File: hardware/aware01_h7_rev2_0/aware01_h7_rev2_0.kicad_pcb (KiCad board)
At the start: 4 copper layers, 46 x 110 mm, 155 parts, among them IC1 587-2054-127F, IC2 587-2054-127F, IC3 587-2054-127F, IC4 587-2054-127F, IC5 TLV320AIC3204IRHBR, J1 Conn_02x07_Odd_Even, J10 GATE4_IN, J11 CV2_IN, J12 CV3_IN, J13 V/OCT_IN, J14 CV1_IN, J2 Conn_02x05_Odd_Even, J3 InL, J4 InR, J5 OutL, J6 OutR, J7 GATE1_IN, J8 GATE2_IN, J9 GATE3_IN, Q1 MMBT3904, Q2 MMBT3904, Q3 MMBT3904, Q4 MMBT3904, SW1 SW_Push, SW2 SW_Push, U1 LMR50410Y5FQDBVRQ1, U10 NE5532DRG4, U11 NE5532DRG4, U12 OPA2322AIDR, U13 OPA2322AIDR, U2 LM1117MP-3.3, U4 STM32H7A3RITx, U5 LM4040DIM3X-10, U6 10k, U7 10k, U8 10k, U9 10k, Y1 WE-XTAL 24.0MHz 50ppm

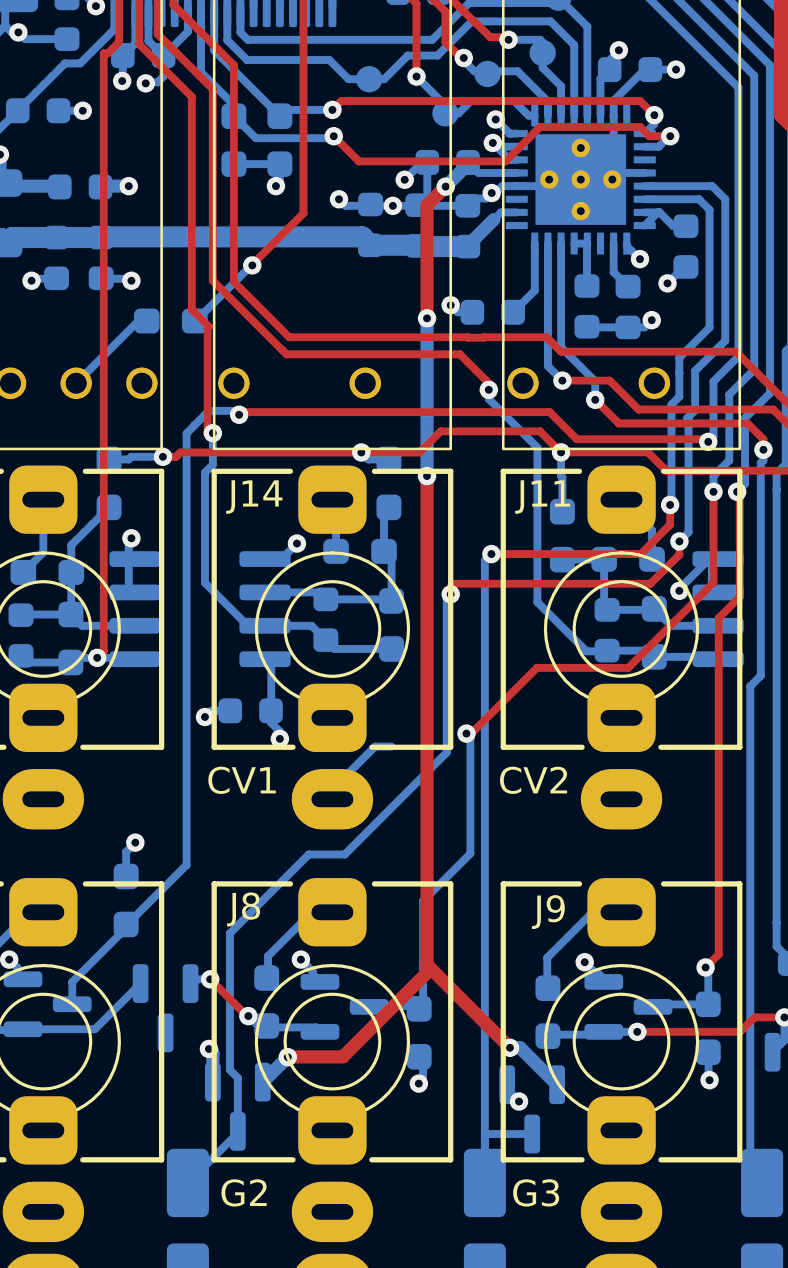
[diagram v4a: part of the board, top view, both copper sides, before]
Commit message: hardware: change clamping reference to codec AVDD
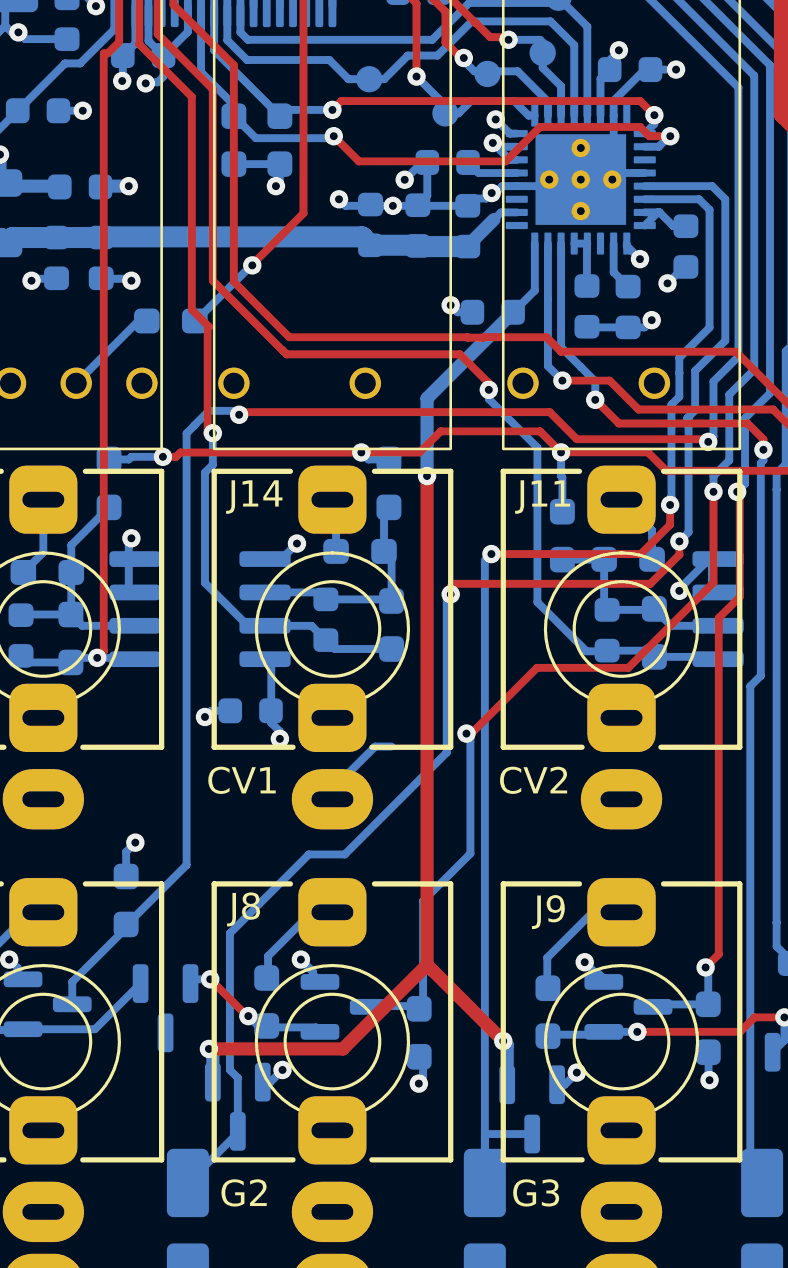
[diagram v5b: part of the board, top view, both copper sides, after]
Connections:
- C38 pad 2: DVDD -> Net-(IC5-DVDD)
- C41 pad 2: Net-(IC5-AVDD) -> AVDD
- D4 pad 1: GND -> AVDD
- D4 pad 2: DVDD -> GND
- D5 pad 1: GND -> AVDD
- D5 pad 2: DVDD -> GND
- IC5 pad 24: Net-(IC5-AVDD) -> AVDD
- IC5 pad 29: DVDD -> Net-(IC5-DVDD)
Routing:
- net DVDD: track 48.3 -> 0.00 mm, vias 5 -> 0
- net AVDD: track 0.00 -> 45.8 mm, vias 0 -> 3
- net Net-(IC5-AVDD): track 2.96 -> 0.00 mm
- net Net-(IC5-DVDD): track 0.00 -> 2.09 mm
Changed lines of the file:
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@@
 	(net 13 "Net-(C23-Pad2)")
 	(net 14 "/I2S1_CK")
-	(net 15 "DVDD")
+	(net 15 "Net-(IC5-DVDD)")
 	(net 16 "Net-(IC5-IN2_L)")
 	(net 17 "/UART_Rx")
-	(net 18 "Net-(IC5-AVDD)")
+	(net 18 "AVDD")
 	(net 19 "Net-(IC5-REF)")
 	(net 20 "/FADER1_IN")
@@
 			(layers "B.Cu" "B.Mask" "B.Paste")
 			(roundrect_rratio 0.25)
-			(net 1 "GND")
+			(net 18 "AVDD")
 			(pinfunction "A")
 			(pintype "passive")
@@
 			(layers "B.Cu" "B.Mask" "B.Paste")
 			(roundrect_rratio 0.25)
-			(net 15 "DVDD")
+			(net 1 "GND")
 			(pinfunction "K")
 			(pintype "passive")
@@
 			(layers "B.Cu" "B.Mask" "B.Paste")
 			(roundrect_rratio 0.25)
-			(net 1 "GND")
+			(net 18 "AVDD")
 			(pinfunction "A")
 			(pintype "passive")
@@
 			(layers "B.Cu" "B.Mask" "B.Paste")
 			(roundrect_rratio 0.25)
-			(net 15 "DVDD")
+			(net 1 "GND")
 			(pinfunction "K")
 			(pintype "passive")
@@
 			(layers "B.Cu" "B.Mask" "B.Paste")
 			(roundrect_rratio 0.25)
-			(net 15 "DVDD")
+			(net 15 "Net-(IC5-DVDD)")
 			(pintype "passive")
 		)
@@
 			(layers "B.Cu" "B.Mask" "B.Paste")
 			(roundrect_rratio 0.125)
-			(net 18 "Net-(IC5-AVDD)")
+			(net 18 "AVDD")
 			(pinfunction "AVDD")
 			(pintype "passive")
@@
 			(layers "B.Cu" "B.Mask" "B.Paste")
 			(roundrect_rratio 0.125)
-			(net 15 "DVDD")
+			(net 15 "Net-(IC5-DVDD)")
 			(pinfunction "DVDD")
 			(pintype "passive")
@@
 			(layers "B.Cu" "B.Mask" "B.Paste")
 			(roundrect_rratio 0.25)
-			(net 18 "Net-(IC5-AVDD)")
+			(net 18 "AVDD")
 			(pintype "passive")
 		)
@@
 	)
 	(via
+		(at 157 130.1)
+		(size 0.7)
+		(drill 0.3)
+		(layers "F.Cu" "B.Cu")
+		(net 1)
+	)
+	(via
 		(at 152.2 100.9)
 		(size 0.7)
@@
 	)
 	(via
-		(at 143 129.2)
-		(size 0.7)
-		(drill 0.3)
-		(layers "F.Cu" "B.Cu")
-		(net 1)
-	)
-	(via
 		(at 168.1 45.1)
 		(size 0.7)
@@
 	)
 	(via
-		(at 140.05 109.76875)
+		(at 145.8 130)
 		(size 0.7)
 		(drill 0.3)
@@
 	)
 	(via
-		(at 160.9 111.76875)
+		(at 140.05 109.76875)
 		(size 0.7)
 		(drill 0.3)
@@
 	)
 	(via
-		(at 154.8 131.2)
+		(at 160.9 111.76875)
 		(size 0.7)
 		(drill 0.3)
@@
 	)
 	(segment
+		(start 156.25 130.5625)
+		(end 156.5375 130.5625)
+		(width 0.3)
+		(layer "B.Cu")
+		(net 1)
+	)
+	(segment
 		(start 167.2 142.1)
 		(end 166.861 142.439)
@@
 	)
 	(segment
+		(start 156.5375 130.5625)
+		(end 157 130.1)
+		(width 0.3)
+		(layer "B.Cu")
+		(net 1)
+	)
+	(segment
 		(start 149.95 117.69375)
 		(end 149.325 117.69375)
@@
 	)
 	(segment
-		(start 154.35 130.75)
-		(end 154.8 131.2)
-		(width 0.3)
-		(layer "B.Cu")
-		(net 1)
-	)
-	(segment
 		(start 149.3 71.575)
 		(end 148.275 71.575)
@@
 	)
 	(segment
-		(start 154.35 130.5625)
-		(end 154.35 130.75)
-		(width 0.3)
-		(layer "B.Cu")
-		(net 1)
-	)
-	(segment
 		(start 148.2 97.11875)
 		(end 147.95 96.86875)
@@
 	)
 	(segment
-		(start 153.760942 96.631093)
-		(end 153.900228 96.631093)
+		(start 145.3375 130.4625)
+		(end 145.8 130)
 		(width 0.3)
 		(layer "B.Cu")
@@
 	)
 	(segment
-		(start 168.875 61.6)
-		(end 168.875 62.225)
+		(start 153.760942 96.631093)
+		(end 153.900228 96.631093)
 		(width 0.3)
 		(layer "B.Cu")
@@
 	)
 	(segment
-		(start 143 129.2)
-		(end 143.15 129.35)
-		(width 0.5)
+		(start 168.875 61.6)
+		(end 168.875 62.225)
+		(width 0.3)
 		(layer "B.Cu")
 		(net 1)
@@
 	)
 	(segment
-		(start 143.15 129.35)
-		(end 143.15 130.4625)
-		(width 0.5)
-		(layer "B.Cu")
-		(net 1)
-	)
-	(segment
 		(start 153.552302 96.839733)
 		(end 153.129017 96.839733)
@@
 	)
 	(segment
+		(start 145.05 130.4625)
+		(end 145.3375 130.4625)
+		(width 0.3)
+		(layer "B.Cu")
+		(net 1)
+	)
+	(segment
 		(start 147.575 73.74375)
 		(end 147.7 73.61875)
@@
 	)
 	(segment
-		(start 146.0125 129.5)
-		(end 148.1 129.5)
-		(width 0.5)
-		(layer "F.Cu")
-		(net 15)
-	)
-	(segment
-		(start 154.45625 129.15625)
-		(end 151.3 126)
-		(width 0.5)
-		(layer "F.Cu")
-		(net 15)
-	)
-	(segment
-		(start 151.3 126.3)
-		(end 151.3 126)
-		(width 0.5)
-		(layer "F.Cu")
-		(net 15)
-	)
-	(segment
-		(start 152.01 96.385846)
-		(end 151.3 97.095846)
-		(width 0.5)
-		(layer "F.Cu")
-		(net 15)
-	)
-	(segment
-		(start 146 129.5125)
-		(end 146.0125 129.5)
-		(width 0.5)
-		(layer "F.Cu")
-		(net 15)
-	)
-	(segment
-		(start 148.1 129.5)
-		(end 151.3 126.3)
-		(width 0.5)
-		(layer "F.Cu")
-		(net 15)
-	)
-	(segment
-		(start 151.3 97.095846)
-		(end 151.3 101.4)
-		(width 0.5)
-		(layer "F.Cu")
-		(net 15)
-	)
-	(segment
-		(start 151.3 107.4)
-		(end 151.3 126)
-		(width 0.5)
-		(layer "F.Cu")
-		(net 15)
-	)
-	(via
-		(at 154.45625 129.15625)
-		(size 0.7)
-		(drill 0.3)
-		(layers "F.Cu" "B.Cu")
-		(net 15)
-	)
-	(via
-		(at 152.01 96.385846)
-		(size 0.7)
-		(drill 0.3)
-		(layers "F.Cu" "B.Cu")
-		(net 15)
-	)
-	(via
-		(at 151.3 101.4)
-		(size 0.7)
-		(drill 0.3)
-		(layers "F.Cu" "B.Cu")
-		(net 15)
-	)
-	(via
-		(at 151.3 107.4)
-		(size 0.7)
-		(drill 0.3)
-		(layers "F.Cu" "B.Cu")
-		(net 15)
-	)
-	(via
-		(at 146 129.5125)
-		(size 0.7)
-		(drill 0.3)
-		(layers "F.Cu" "B.Cu")
-		(net 15)
-	)
-	(segment
-		(start 152.01 96.385846)
-		(end 152.86 95.535846)
-		(width 0.5)
-		(layer "B.Cu")
-		(net 15)
-	)
-	(segment
-		(start 154.45625 129.15625)
-		(end 154.84375 129.15625)
-		(width 0.5)
-		(layer "B.Cu")
-		(net 15)
-	)
-	(segment
-		(start 151.3 101.4)
-		(end 151.3 107.4)
-		(width 0.5)
-		(layer "B.Cu")
-		(net 15)
-	)
-	(segment
 		(start 154.715 95.86875)
 		(end 153.26 95.86875)
@@
 	)
 	(segment
-		(start 146 129.5125)
-		(end 145.05 130.4625)
-		(width 0.5)
-		(layer "B.Cu")
-		(net 15)
-	)
-	(segment
-		(start 154.84375 129.15625)
-		(end 156.25 130.5625)
-		(width 0.5)
-		(layer "B.Cu")
-		(net 15)
-	)
-	(segment
 		(start 153.26 95.86875)
 		(end 152.86 95.46875)
@@
 	)
 	(segment
+		(start 151.3 126)
+		(end 151.5 126.2)
+		(width 0.5)
+		(layer "F.Cu")
+		(net 18)
+	)
+	(segment
+		(start 151.3 126)
+		(end 148.1 129.2)
+		(width 0.5)
+		(layer "F.Cu")
+		(net 18)
+	)
+	(segment
+		(start 151.5 126.2)
+		(end 154.2 128.9)
+		(width 0.5)
+		(layer "F.Cu")
+		(net 18)
+	)
+	(segment
+		(start 148.1 129.2)
+		(end 143 129.2)
+		(width 0.5)
+		(layer "F.Cu")
+		(net 18)
+	)
+	(segment
+		(start 151.3 107.4)
+		(end 151.3 126)
+		(width 0.5)
+		(layer "F.Cu")
+		(net 18)
+	)
+	(via
+		(at 143 129.2)
+		(size 0.7)
+		(drill 0.3)
+		(layers "F.Cu" "B.Cu")
+		(net 18)
+	)
+	(via
+		(at 154.2 128.9)
+		(size 0.7)
+		(drill 0.3)
+		(layers "F.Cu" "B.Cu")
+		(net 18)
+	)
+	(via
+		(at 151.3 107.4)
+		(size 0.7)
+		(drill 0.3)
+		(layers "F.Cu" "B.Cu")
+		(net 18)
+	)
+	(segment
+		(start 154.35 129.05)
+		(end 154.35 130.4625)
+		(width 0.5)
+		(layer "B.Cu")
+		(net 18)
+	)
+	(segment
+		(start 143.15 129.35)
+		(end 143.15 130.4625)
+		(width 0.5)
+		(layer "B.Cu")
+		(net 18)
+	)
+	(segment
+		(start 151.3 104.44375)
+		(end 151.3 107.4)
+		(width 0.5)
+		(layer "B.Cu")
+		(net 18)
+	)
+	(segment
+		(start 143 129.2)
+		(end 143.15 129.35)
+		(width 0.5)
+		(layer "B.Cu")
+		(net 18)
+	)
+	(segment
+		(start 154.2 128.9)
+		(end 154.35 129.05)
+		(width 0.5)
+		(layer "B.Cu")
+		(net 18)
+	)
+	(segment
 		(start 155.4 98.55375)
 		(end 155.4 100.34375)
@@
 		(layer "B.Cu")
 		(net 18)
+	)
+	(segment
+		(start 154.575 101.16875)
+		(end 151.3 104.44375)
+		(width 0.5)
+		(layer "B.Cu")
+		(net 18)

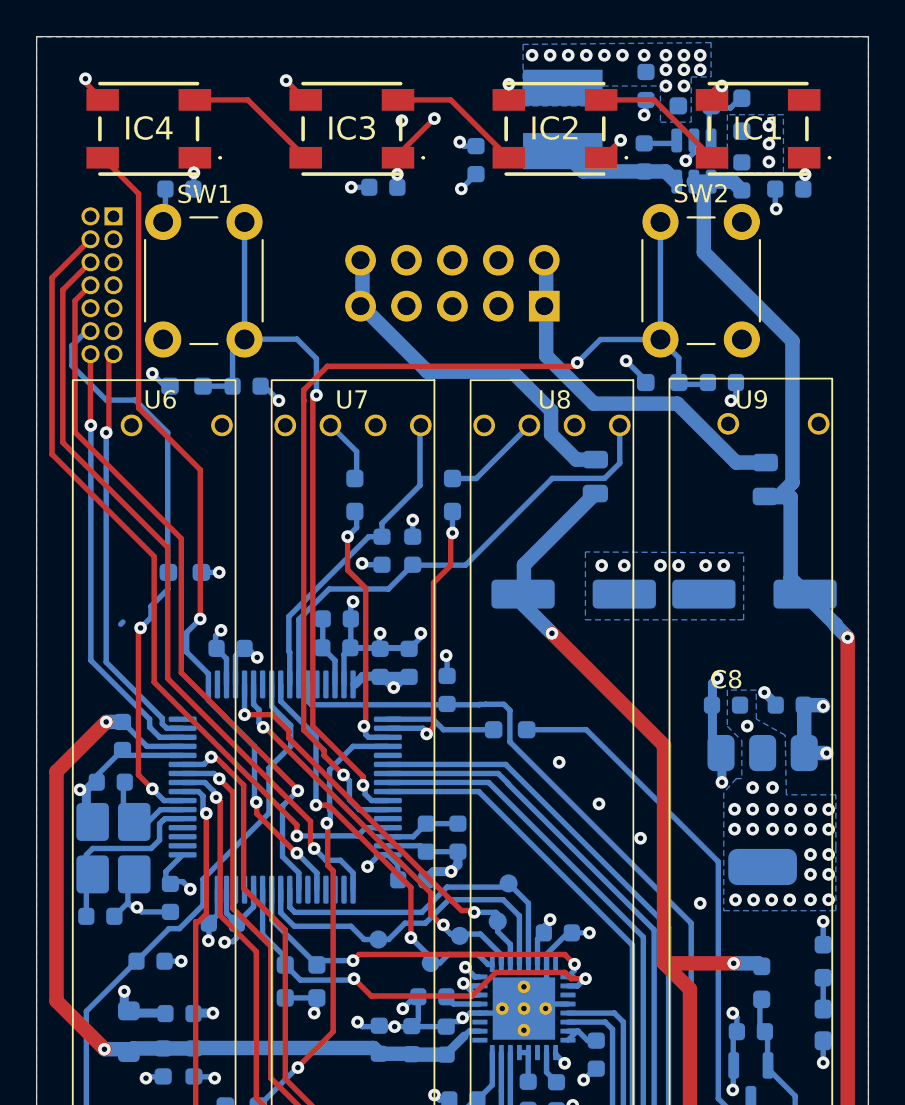
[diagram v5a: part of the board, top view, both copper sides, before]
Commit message: hardware: add levelshifter for WS2812
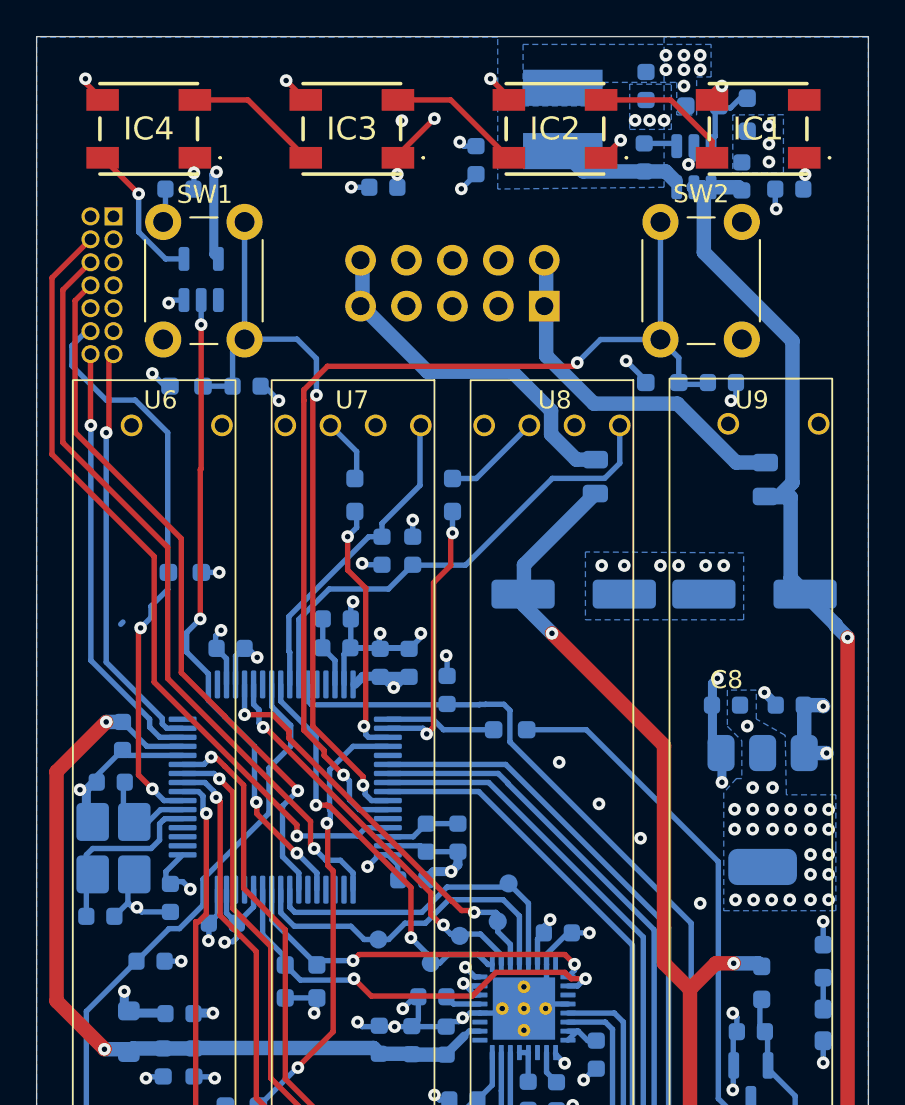
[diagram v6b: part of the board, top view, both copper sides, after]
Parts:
- added U3: 74AHCT1G14DBVRG4, Package_TO_SOT_SMD:SOT-23-5, B.Cu at (139.3, 55.8)
- moved R2 0.41 mm to (167.0, 46.2)
- moved U1 0.31 mm to (166.6, 49.6)
- moved R3 0.30 mm to (169.5, 46.7)
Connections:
- IC4 pad 4: /RGB_LED_DATA -> Net-(IC4-DIN)
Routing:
- net /RGB_LED_DATA: track 46.1 -> 36.0 mm, vias 3 -> 4
- net Net-(IC4-DIN): track 0.00 -> 8.05 mm, vias 0 -> 1
- net +5V: track 15.6 -> 20.6 mm, vias 23 -> 16
- net +12V: track 138.6 -> 137.4 mm
- net GND: track 135.3 -> 136.2 mm, vias 76 -> 79
- net -12V: track 118.3 -> 117.5 mm
- net Net-(IC1-DIN): track 7.46 -> 8.00 mm
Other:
- board text removed: "-12V"

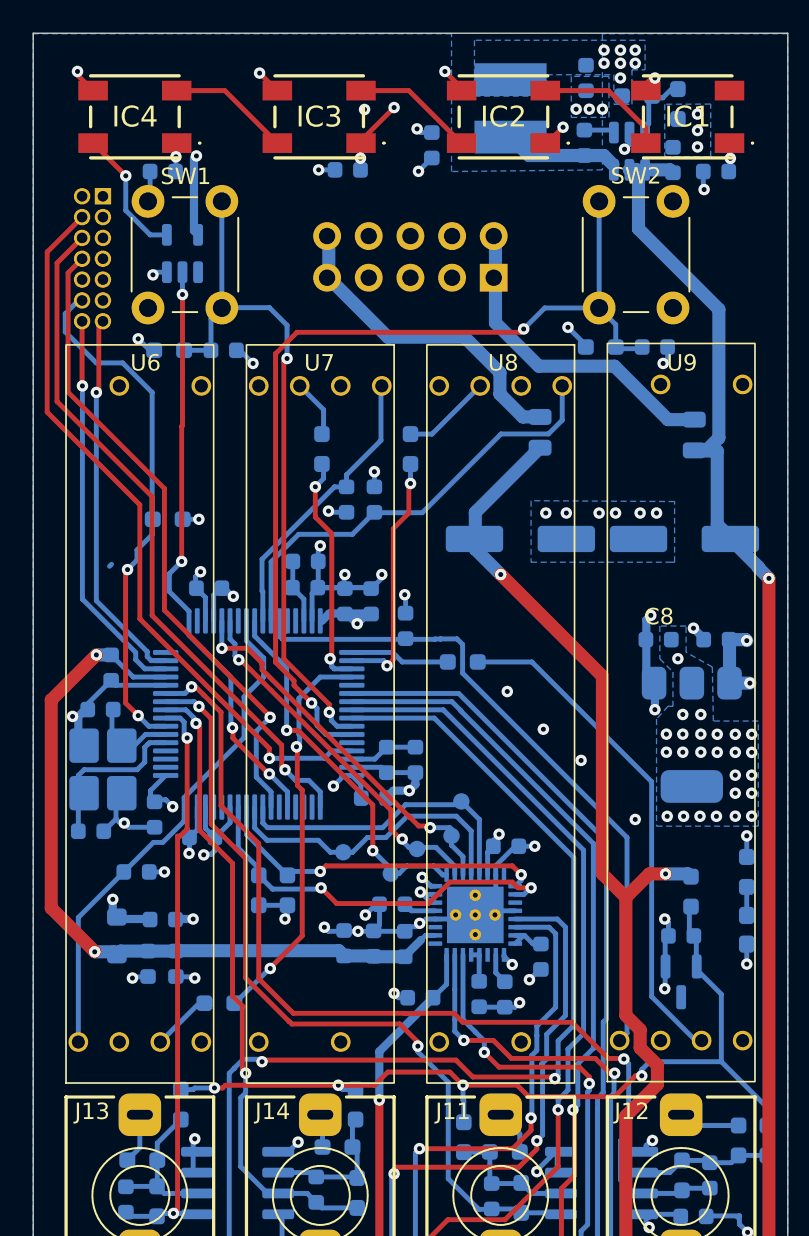
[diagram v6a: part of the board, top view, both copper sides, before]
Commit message: hardware: adjust buck layout
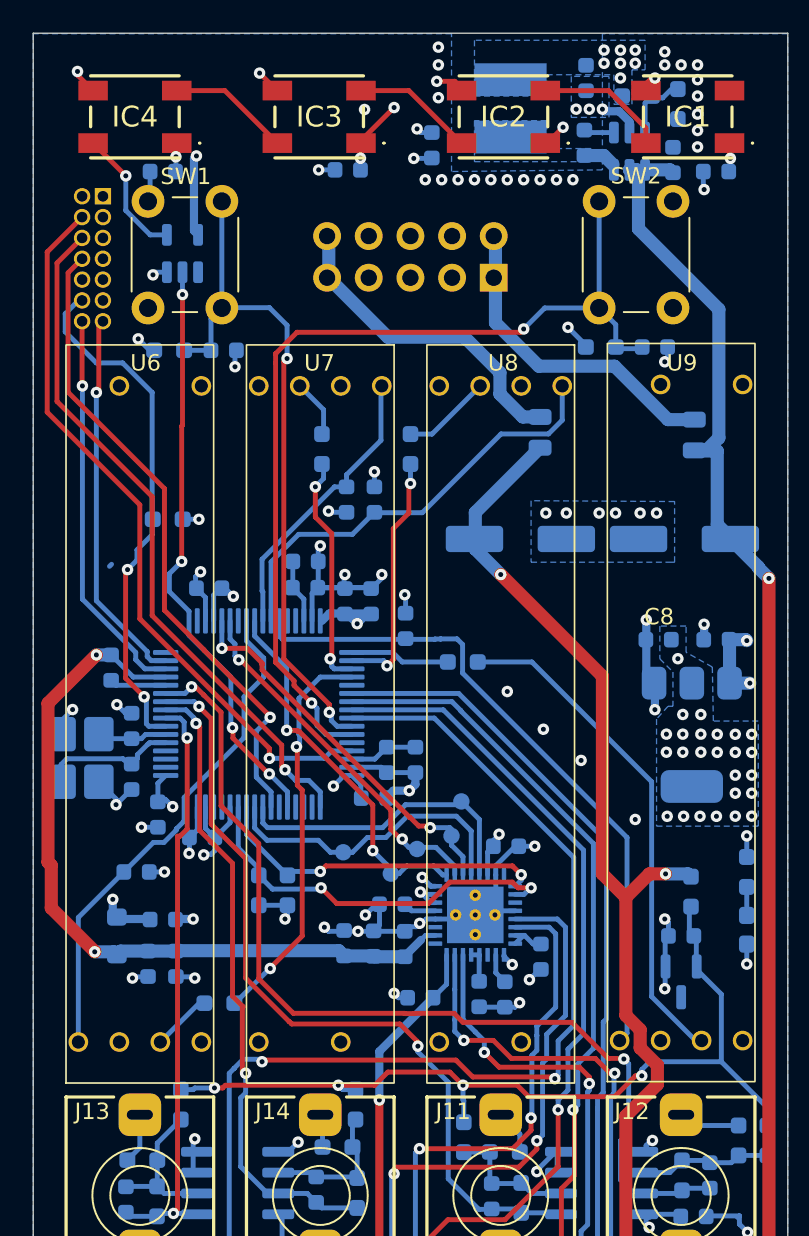
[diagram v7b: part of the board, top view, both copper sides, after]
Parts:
- moved C17 4.14 mm to (136.2, 87.7), turned to -90 degrees
- moved C21 2.15 mm to (136.2, 84.6), turned to 90 degrees
- moved Y1 1.57 mm to (133.1, 86.5)
- moved C3 0.20 mm to (137.8, 90.0)
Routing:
- net Net-(U1-SW): track 6.95 -> 1.98 mm
- net GND: track 136.2 -> 132.9 mm, vias 79 -> 99
- net Net-(U4-PH0): track 10.1 -> 8.46 mm
- net Net-(U4-PH1): track 5.44 -> 4.30 mm
- net +3.3V: track 45.7 -> 44.9 mm
- added copper zone on B.Cu, net Net-(U1-SW)
